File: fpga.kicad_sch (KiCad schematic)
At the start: 54 parts, among them U1 MACHXO2-1200HC-4TG100C, U2 TDC_7200, X1 16MHz

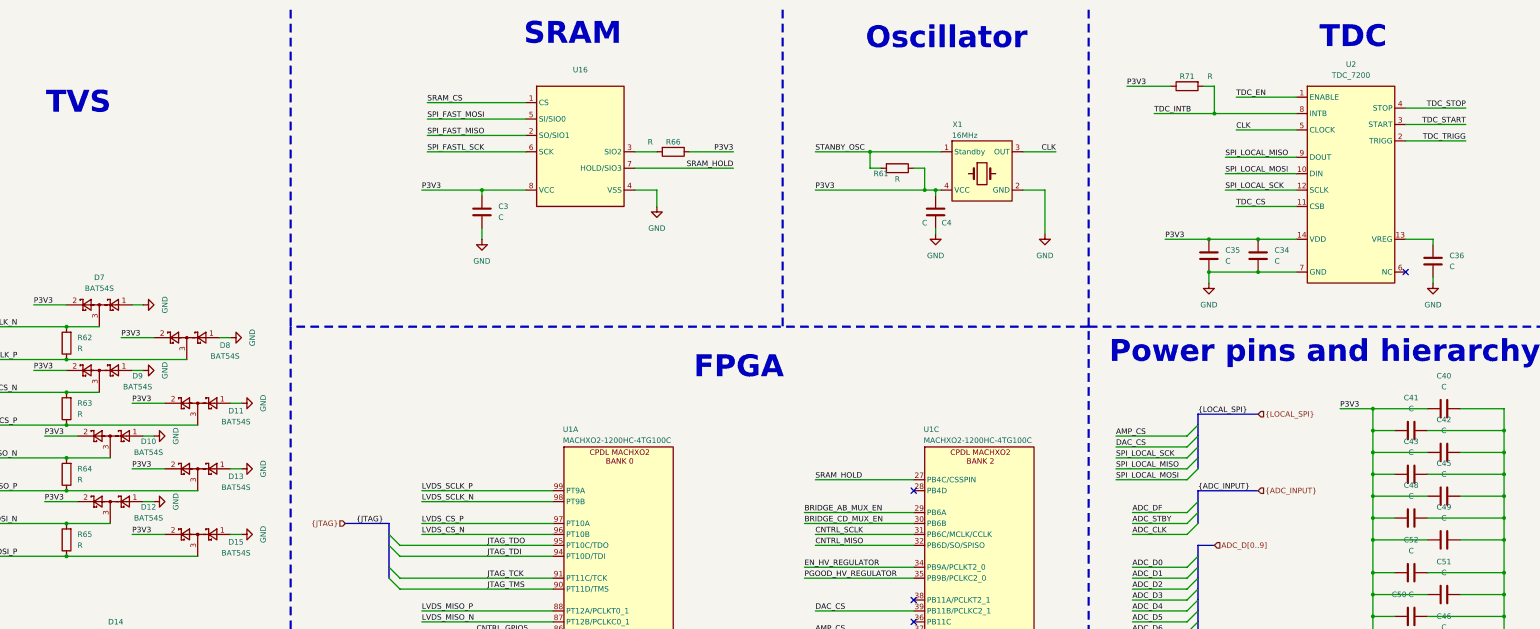
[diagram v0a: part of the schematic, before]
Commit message: most values in schematic filled corrected footprint mistake
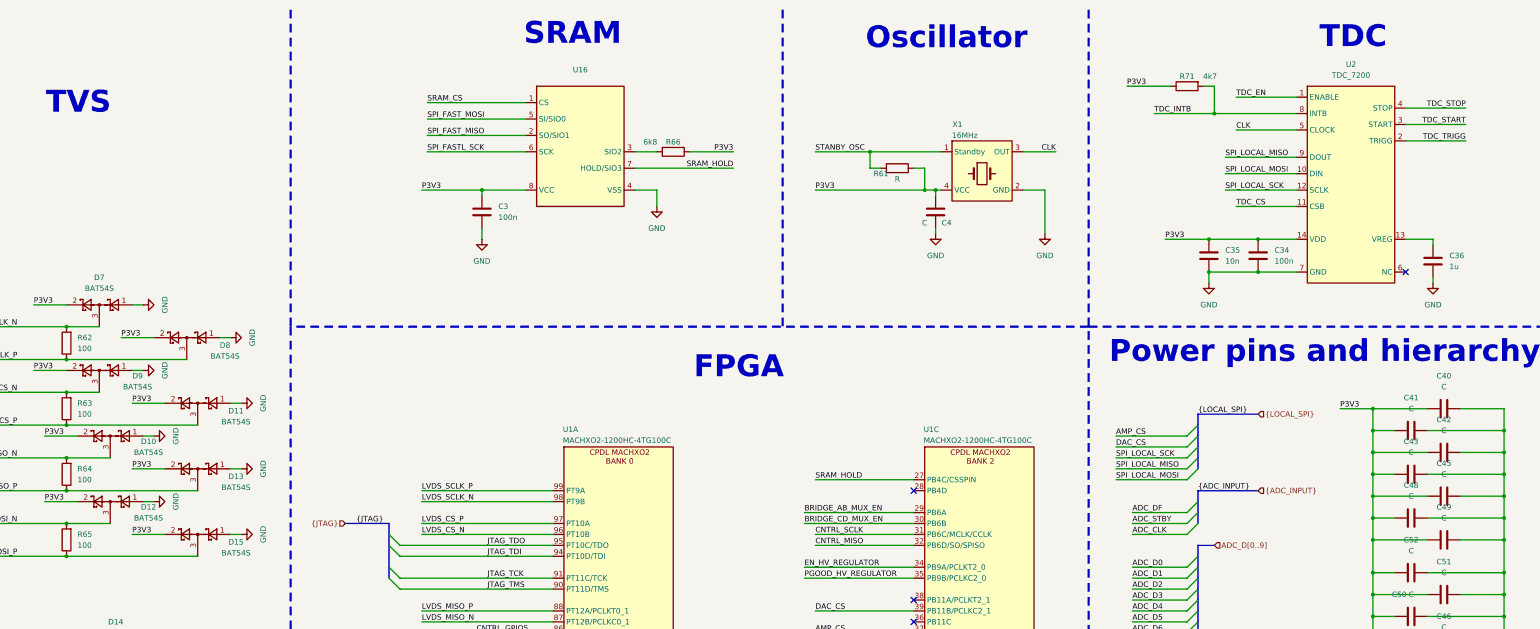
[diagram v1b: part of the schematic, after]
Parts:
- C3, C34: value C -> 100n
- C35: value C -> 10n
- C36: value C -> 1u
- D7: footprint Package_TO_SOT_SMD:SOT-23 -> Package_TO_SOT_SMD:SOT-23-3
- R62, R63, R64, R65: value R -> 100
- R66: value R -> 6k8
- R71: value R -> 4k7
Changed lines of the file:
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@@
 			)
 		)
-		(property "Value" "C"
+		(property "Value" "10n"
 			(at 331.47 71.1199 0)
 			(effects
@@
 			)
 		)
-		(property "Footprint" "Package_TO_SOT_SMD:SOT-23"
+		(property "Footprint" "Package_TO_SOT_SMD:SOT-23-3"
 			(at 67.945 78.105 0)
 			(effects
@@
 			)
 		)
-		(property "Value" "R"
+		(property "Value" "100"
 			(at 64.77 91.4399 0)
 			(effects
@@
 			)
 		)
-		(property "Value" "R"
+		(property "Value" "100"
 			(at 64.77 121.9199 0)
 			(effects
@@
 			)
 		)
-		(property "Value" "R"
+		(property "Value" "6k8"
 			(at 197.866 43.434 90)
 			(effects
@@
 			)
 		)
-		(property "Value" "C"
+		(property "Value" "100n"
 			(at 162.56 60.9599 0)
 			(effects
@@
 			)
 		)
-		(property "Value" "C"
+		(property "Value" "1u"
 			(at 383.54 72.3899 0)
 			(effects
@@
 			)
 		)
-		(property "Value" "R"
+		(property "Value" "4k7"
 			(at 327.914 28.194 90)
 			(effects
@@
 			)
 		)
-		(property "Value" "R"
+		(property "Value" "100"
 			(at 64.77 106.6799 0)
 			(effects
@@
 			)
 		)
-		(property "Value" "C"
+		(property "Value" "100n"
 			(at 342.9 71.1199 0)
 			(effects
@@
 			)
 		)
-		(property "Value" "R"
+		(property "Value" "100"
 			(at 64.77 137.1599 0)
 			(effects

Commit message: V2 finished
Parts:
- removed C37, C38, C39, C40, C41, C42, C43, C44, C45, C46, C47, C48, C49, C50, C51, C52: C, Capacitor_SMD:C_0603_1608Metric_Pad1.08x0.95mm_HandSolder, symbol Device:C
- removed D10, D11, D12, D13, D15, D8, D9: BAT54S, Package_TO_SOT_SMD:SOT-23, symbol Diode:BAT54S
- removed D7: BAT54S, Package_TO_SOT_SMD:SOT-23-3, symbol Diode:BAT54S
- removed R85: 12, Resistor_SMD:R_0603_1608Metric, symbol Device:R
- removed U1: MACHXO2-1200HC-4TG100C, Package_QFP:TQFP-100_14x14mm_P0.5mm, symbol 10_ICs:LCMXO2-1200HC-4TG100C
- added R88: R, Capacitor_SMD:C_0603_1608Metric_Pad1.08x0.95mm_HandSolder, symbol Device:R
- added U1, U24, U26, U27: USBLC6-2SC6, Package_TO_SOT_SMD:SOT-23-6, symbol Power_Protection:USBLC6-2SC6
- added X2: LCMXO-7000HC-6TG-144C, Package_QFP:TQFP-144_20x20mm_P0.5mm, symbol 10_ICs:LCMXO-7000HC-6TG-144C
- R60: value R -> 12; footprint Capacitor_SMD:C_0603_1608Metric_Pad1.08x0.95mm_HandSolder -> Resistor_SMD:R_0603_1608Metric
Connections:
- net ADC_CLK: now also X2.82 (PR18A)
- net ADC_D0: now also X2.84 (PR17A)
- net ADC_D1: now also X2.85 (PR16B)
- net ADC_D2: now also X2.86 (PR16A)
- net ADC_D3: now also X2.87 (PR15B)
- net ADC_D4: now also X2.89 (PR15A)
- net ADC_D5: now also X2.91 (PR12B/PCLKC1_0)
- net ADC_D6: now also X2.92 (PR12A/PCLKT1_0)
- net ADC_D7: now also X2.93 (PR11B)
- net ADC_D8: now also X2.94 (PR11A)
- net ADC_D9: now also X2.95 (PR9B)
- net ADC_DF: now also X2.96 (PR9A)
- net ADC_STBY: now also X2.83 (PR17B)
- net AMP_CS: now also X2.43 (PB9B)
- net BRIDGE_AB_MUX_EN: now also X2.60 (PB29B)
- net BRIDGE_A_HI: now also X2.107 (PR2A/R_GPLL_FB)
- net BRIDGE_A_LO: now also X2.106 (PR2B/R_GPLLC_FB)
- net BRIDGE_A_SEL: now also X2.48 (PB13B)
- net BRIDGE_B_HI: now also X2.105 (PR3A/R_GPLLT_IN)
- net BRIDGE_B_LO: now also X2.104 (PR3B/R_GPLLC_IN)
- net BRIDGE_B_SEL: now also X2.50 (PB16B/PCLKC2_0)
- net BRIDGE_CD_MUX_EN: now also X2.62 (PB31B)
- net BRIDGE_C_HI: now also X2.74 (PR24A)
- net BRIDGE_C_LO: now also X2.73 (PR24B)
- net BRIDGE_C_SEL: now also X2.54 (PB18B)
- net BRIDGE_D_HI: now also X2.76 (PR23A)
- net BRIDGE_D_LO: now also X2.75 (PR23B)
- net BRIDGE_D_SEL: now also X2.56 (PB23B/PCLKC2_1)
- net CLK: now also X2.3 (PL4A/L_GPLLT_IN); no longer U2.5 (CLOCK)
- net CNTRL_CS: now also X2.114 (PT33A)
- net CNTRL_GPIO0: now also X2.109 (PT36D/DONE)
- net CNTRL_GPIO1: now also X2.110 (PT36C/INITN)
- net CNTRL_GPIO2: now also X2.111 (PT35B); no longer R60.2
- net CNTRL_GPIO3: now also X2.112 (PT35A)
- net CNTRL_GPIO4: now also X2.125 (PT22D/SDA/PCLKC0_0)
- net CNTRL_GPIO5: now also X2.126 (PT22C/SCL/PCLKT0_0)
- net CNTRL_MISO: now also X2.115 (PT28B)
- net CNTRL_MOSI: now also X2.113 (PT33B)
- net CNTRL_SCLK: now also X2.117 (PT28A)
- net COMP_SHT: now also X2.99 (PR5B)
- net DAC_CS: now also X2.41 (PB6B)
- net EN_HV_REGULATOR: now also X2.38 (PB4A)
- net GND: now also U1.2 (GND), U24.2 (GND), U26.2 (GND), U27.2 (GND), X2.101 (GND), X2.116 (GND), X2.124 (GND), X2.134 (GND), X2.18 (GND), X2.29 (GND), X2.46 (GND), X2.53 (GND), X2.64 (GND), X2.8 (GND), X2.80 (GND), X2.90 (GND)
- net JTAG_TCK: now also X2.131 (PT14C/TCK)
- net JTAG_TDI: now also X2.136 (PT14D/TDI)
- net JTAG_TDO: now also X2.137 (PT14C/TDO)
- net JTAG_TMS: now also X2.130 (PT17D/TMS)
- net LVDS_CS_N: now also U1.1 (I/O1); no longer R63.2
- net LVDS_CS_P: now also U1.3 (I/O2); no longer R63.1
- net LVDS_MISO_N: now also U26.1 (I/O1); no longer R64.2
- net LVDS_MISO_P: now also U26.3 (I/O2); no longer R64.1
- net LVDS_MOSI_N: now also U27.1 (I/O1); no longer R65.2
- net LVDS_MOSI_P: now also U27.3 (I/O2); no longer R65.1
- net LVDS_SCLK_N: now also U24.1 (I/O1); no longer R62.2
- net LVDS_SCLK_P: now also U24.3 (I/O2); no longer R62.1
- net P3V3: now also R88.1, U1.5 (VBUS), U24.5 (VBUS), U26.5 (VBUS), U27.5 (VBUS), X2.108 (VCC), X2.144 (VCC), X2.36 (VCC), X2.72 (VCC); no longer R60.1
- net PGOOD_HV_REGULATOR: now also X2.39 (PB4B)
- net SPI_FASTL_SCK: now also X2.27 (PL22A/PCLKT3_0)
- net SPI_FAST_MISO: now also X2.34 (PL25A)
- net SPI_FAST_MOSI: now also X2.28 (PL22B/PCLKC3_0)
- net SPI_LOCAL_MISO: now also R60.1; no longer R83.1
- net SPI_LOCAL_SCK: now also R83.1
- net SRAM_CS: now also X2.33 (PL24B)
- net SRAM_HOLD: now also X2.32 (PL24A)
- net STANBY_OSC: now also X2.1 (PL3A/L_GPLLT_FB)
- net STOP_SIGNAL: now also X2.103 (PR4C)
- net TDC_CS: now also X2.9 (PL8A)
- net TDC_EN: now also X2.24 (PL17B)
- net TDC_INTB: now also X2.15 (PL11A)
- net TDC_START: now also X2.22 (PL15B)
- net TDC_STOP: now also X2.21 (PL15A)
- net TDC_TRIGG: now also X2.23 (PL17A)
- net at R84.2: now also X2.12 (PL9B)
- net at R83.2: now also X2.5 (PL6A/PCLKT5_0)
- new net: R60.2, X2.10 (PL8B)
- new net: R88.2, X2.119 (PT27D/PROGRAMN)
- new net CHARGE_AMP_SHT: X2.65 (PB35A)
- new net LVDS_CS_TVS_N: R63.2, U1.6 (I/O1), X2.140 (PT10B)
- new net LVDS_CS_TVS_P: R63.1, U1.4 (I/O2), X2.141 (PT10A)
- new net LVDS_MISO_TVS_N: R64.2, U26.6 (I/O1), X2.138 (PT11B)
- new net LVDS_MISO_TVS_P: R64.1, U26.4 (I/O2), X2.139 (PT11A)
- new net LVDS_MOSI_TVS_N: R65.2, U27.6 (I/O1), X2.132 (PT15B)
- new net LVDS_MOSI_TVS_P: R65.1, U27.4 (I/O2), X2.133 (PT15A)
- new net LVDS_SCLK_TVS_N: R62.1, U24.6 (I/O1), X2.142 (PT9B)
- new net LVDS_SCLK_TVS_P: R62.2, U24.4 (I/O2), X2.143 (PT9A)
- new net P3V3_A_EN: X2.68 (PB37A)
- new net TDC_CLK: U2.5 (CLOCK), X2.19 (PL12A/PCLKT4_0)
- new net fpgaBankPower/VCCIO0: X2.118 (VCCIO0), X2.123 (VCCIO0), X2.135 (VCCIO0)
- new net fpgaBankPower/VCCIO1: X2.102 (VCCIO1), X2.79 (VCCIO1), X2.88 (VCCIO1)
- new net fpgaBankPower/VCCIO2: X2.37 (VCCIO2), X2.51 (VCCIO2), X2.66 (VCCIO2)
- new net fpgaBankPower/VCCIO3: X2.30 (VCCIO3)
- new net fpgaBankPower/VCCIO4: X2.16 (VCCIO4)
- new net fpgaBankPower/VCCIO5: X2.7 (VCCIO5)
- no-connect marks 11 -> 42
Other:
- added sheet fpgaBankPower (fpgaBankPower.kicad_sch)
- moved on the sheet: C3, C4, D14, D16, D17, D18, R61, R62, R63, R64, R65, R66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
